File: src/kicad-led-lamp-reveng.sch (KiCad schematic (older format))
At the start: 18 parts, among them J1 AC2, J2 AC1, J3 L+, J4 L-, SW1 SW_Push_SPDT

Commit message: Finished pcb layout
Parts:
- C1: footprint (none) -> igorkelvin:C_Polyester_11.20mm_4.9mm
- C2: footprint (none) -> igorkelvin:C_Polyester_21.80mm_7.10mm
- D1, D3, D4, D5, D6: footprint Resistor_THT:R_Axial_DIN0207_L6.3mm_D2.5mm_P7.62mm_Horizontal -> igorkelvin:DIODE_Axial_DIN0207_L6.3mm_D2.5mm_P7.62mm_Horizontal
- J1, J2, J3, J4: footprint (none) -> Connector_PinHeader_2.54mm:PinHeader_1x01_P2.54mm_Vertical
- SW1: footprint (none) -> igorkelvin:Switch_4-Way
- renumbered R3 to R1, R1 to R3
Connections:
- net at C1.2, C2.2, D1.1 (K)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: no longer D5.2 (A), R4.2
- new net: D5.2 (A), R4.2
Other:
- moved on the sheet: C1, C2, C3, D1, D2, D3, D4, D5, D6, J1, J2, J3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

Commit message: Schematics rearrangement, changed C3 polarity and Rev1 for pcb & sch
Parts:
- C1: value 220nF_400V_Polyester -> 220nF
- C2: value 1uF_400V_Polyester -> 1uF
- C3: value 6.8uF_400V_Electrolytic -> 6.8uF
- D2: value LED_ALT -> LED
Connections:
- net at D1.2 (A), D2.1 (K), J4.1 (Pin_1)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: now also C3.2, D3.1 (K); no longer C3.1, D3.2 (A)
- net at D4.1 (K), D6.1 (K), J3.1 (Pin_1)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: now also C3.1; no longer C3.2
- net at D4.2 (A), J2.1 (Pin_1): now also D3.2 (A); no longer D3.1 (K)
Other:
- moved on the sheet: C1, C2, C3, D1, D2, D3, D4, D5, D6, J1, J2, J3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

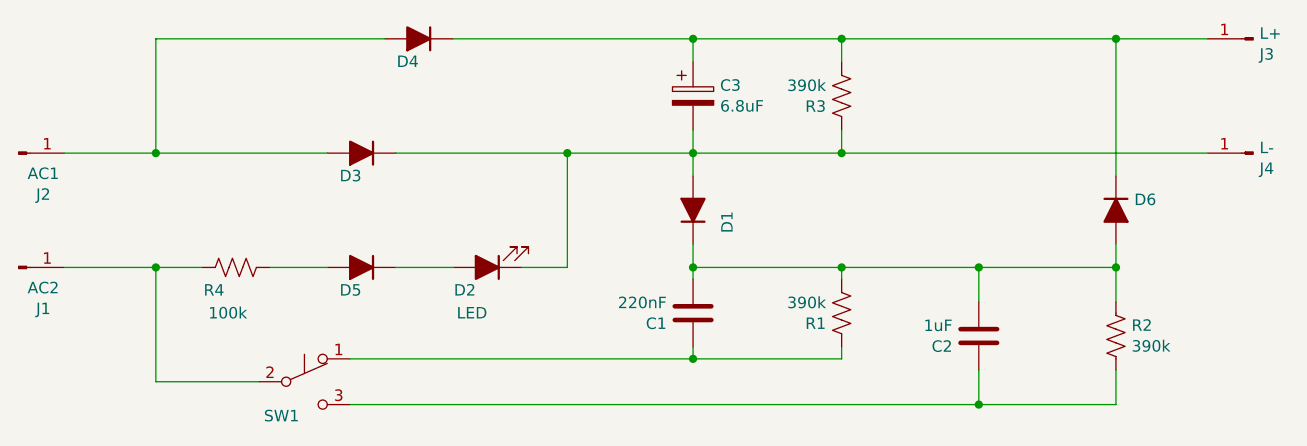
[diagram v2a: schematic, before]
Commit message: Corrected D3 and PCB filled zones
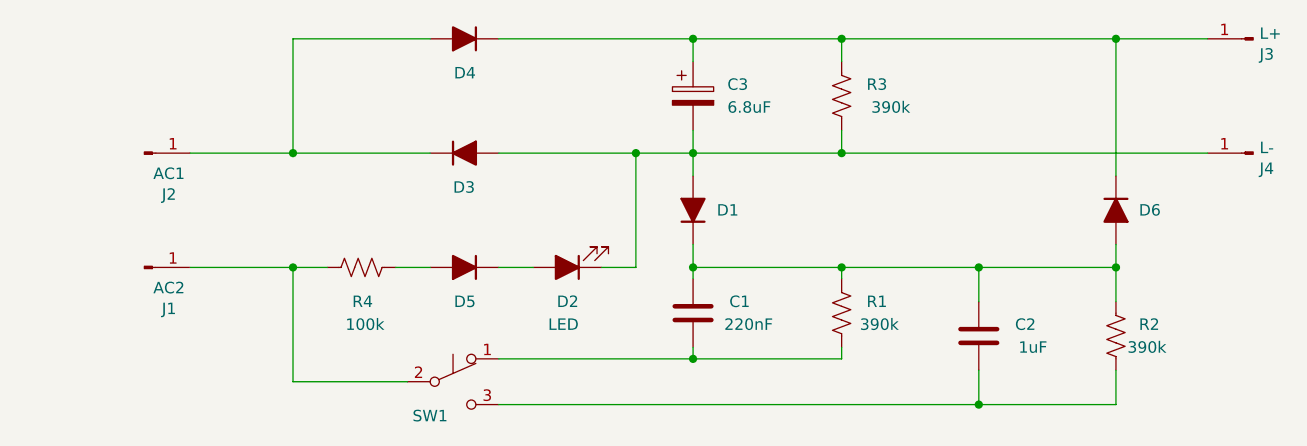
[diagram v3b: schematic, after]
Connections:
- net at C3.2, D1.2 (A), D2.1 (K)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: now also D3.2 (A); no longer D3.1 (K)
- net at D4.2 (A), J2.1 (Pin_1): now also D3.1 (K); no longer D3.2 (A)
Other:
- moved on the sheet: D2, D3, D4, D5, J1, J2, R4, SW1
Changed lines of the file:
@@
 Title "LED Lamp Rev. Engineering"
 Date "2020-08-04"
-Rev "0"
+Rev "1"
 Comp "CEFET/RJ"
 Comment1 "Igor Kelvin <igorkelvin@gmail.com>"
@@
 L Device:D_ALT D3
 U 1 1 5F298B6A
-P 3350 2450
-F 0 "D3" H 3350 2550 50  0000 L CNN
-F 1 "1N4007" V 3395 2530 50  0001 L CNN
-F 2 "igorkelvin:DIODE_Axial_DIN0207_L6.3mm_D2.5mm_P7.62mm_Horizontal" H 3350 2450 50  0001 C CNN
-F 3 "~" H 3350 2450 50  0001 C CNN
-	1    3350 2450
-	-1   0    0    1
+P 3800 2450
+F 0 "D3" H 3750 2300 50  0000 L CNN
+F 1 "1N4007" V 3845 2530 50  0001 L CNN
+F 2 "igorkelvin:DIODE_Axial_DIN0207_L6.3mm_D2.5mm_P7.62mm_Horizontal" H 3800 2450 50  0001 C CNN
+F 3 "~" H 3800 2450 50  0001 C CNN
+	1    3800 2450
+	1    0    0    -1
 $EndComp
 $Comp
@@
 U 1 1 5F29AE02
 P 5450 3150
-F 0 "R1" H 5518 3196 50  0000 L CNN
-F 1 "390k" H 5518 3105 50  0000 L CNN
+F 0 "R1" H 5250 3100 50  0000 L CNN
+F 1 "390k" H 5200 3200 50  0000 L CNN
 F 2 "Resistor_THT:R_Axial_DIN0207_L6.3mm_D2.5mm_P7.62mm_Horizontal" V 5490 3140 50  0001 C CNN
 F 3 "~" H 5450 3150 50  0001 C CNN
@@
 $EndComp
 $Comp
-L Connector:Conn_01x01_Male J2
-U 1 1 5F2EAC7D
-P 1850 2450
-F 0 "J2" H 1958 2631 50  0000 C CNN
-F 1 "AC1" H 1958 2540 50  0000 C CNN
-F 2 "Connector_PinHeader_2.54mm:PinHeader_1x01_P2.54mm_Vertical" H 1850 2450 50  0001 C CNN
-F 3 "~" H 1850 2450 50  0001 C CNN
-	1    1850 2450
-	1    0    0    1
-$EndComp
-$Comp
-L Connector:Conn_01x01_Male J1
-U 1 1 5F2EB389
-P 1850 2950
-F 0 "J1" H 1958 3131 50  0000 C CNN
-F 1 "AC2" H 1958 3040 50  0000 C CNN
-F 2 "Connector_PinHeader_2.54mm:PinHeader_1x01_P2.54mm_Vertical" H 1850 2950 50  0001 C CNN
-F 3 "~" H 1850 2950 50  0001 C CNN
-	1    1850 2950
-	1    0    0    1
-$EndComp
-$Comp
-L Device:LED_ALT D2
-U 1 1 5F29941E
-P 3900 2950
-F 0 "D2" H 3950 3050 50  0000 L CNN
-F 1 "LED" H 3900 3150 50  0000 L CNN
-F 2 "LED_THT:LED_D3.0mm" H 3900 2950 50  0001 C CNN
-F 3 "~" H 3900 2950 50  0001 C CNN
-	1    3900 2950
-	-1   0    0    1
-$EndComp
-$Comp
 L Connector:Conn_01x01_Male J4
 U 1 1 5F2ED558
@@
 U 1 1 5F2984DE
 P 4800 2700
-F 0 "D1" H 4700 2550 50  0000 L CNN
+F 0 "D1" V 4800 2500 50  0000 L CNN
 F 1 "1N4007" H 4700 2450 50  0001 L CNN
 F 2 "igorkelvin:DIODE_Axial_DIN0207_L6.3mm_D2.5mm_P7.62mm_Horizontal" H 4800 2700 50  0001 C CNN
@@
 L Device:R_US R4
 U 1 1 5F29B09B
-P 2800 2950
-F 0 "R4" V 2700 3000 50  0000 L CNN
-F 1 "100k" V 2600 2900 50  0000 L CNN
-F 2 "Resistor_THT:R_Axial_DIN0207_L6.3mm_D2.5mm_P7.62mm_Horizontal" V 2840 2940 50  0001 C CNN
-F 3 "~" H 2800 2950 50  0001 C CNN
-	1    2800 2950
+P 3350 2950
+F 0 "R4" V 3200 2900 50  0000 L CNN
+F 1 "100k" V 3100 2850 50  0000 L CNN
+F 2 "Resistor_THT:R_Axial_DIN0207_L6.3mm_D2.5mm_P7.62mm_Horizontal" V 3390 2940 50  0001 C CNN
+F 3 "~" H 3350 2950 50  0001 C CNN
+	1    3350 2950
 	0    -1   -1   0
 $EndComp
 Wire Wire Line
-	2450 2950 2450 3450
-Wire Wire Line
-	2450 3450 2900 3450
+	3050 2950 3050 3450
+Wire Wire Line
+	3050 3450 3550 3450
 $Comp
 L Device:C C1
 U 1 1 5F297900
 P 4800 3150
-F 0 "C1" H 4915 3196 50  0000 L CNN
-F 1 "220nF" H 4915 3105 50  0000 L CNN
+F 0 "C1" H 4550 3100 50  0000 L CNN
+F 1 "220nF" H 4450 3200 50  0000 L CNN
 F 2 "igorkelvin:C_Polyester_11.20mm_4.9mm" H 4838 3000 50  0001 C CNN
 F 3 "~" H 4800 3150 50  0001 C CNN
@@
 U 1 1 5F298A12
 P 6650 2700
-F 0 "D6" V 6604 2780 50  0000 L CNN
+F 0 "D6" V 6650 2800 50  0000 L CNN
 F 1 "1N4007" V 6695 2780 50  0001 L CNN
 F 2 "igorkelvin:DIODE_Axial_DIN0207_L6.3mm_D2.5mm_P7.62mm_Horizontal" H 6650 2700 50  0001 C CNN
@@
 $EndComp
 $Comp
-L Device:D_ALT D4
-U 1 1 5F2986FE
-P 3600 1950
-F 0 "D4" H 3600 2050 50  0000 L CNN
-F 1 "1N4007" V 3645 2030 50  0001 L CNN
-F 2 "igorkelvin:DIODE_Axial_DIN0207_L6.3mm_D2.5mm_P7.62mm_Horizontal" H 3600 1950 50  0001 C CNN
-F 3 "~" H 3600 1950 50  0001 C CNN
-	1    3600 1950
-	-1   0    0    1
-$EndComp
-Wire Wire Line
-	4250 2450 4800 2450
-Wire Wire Line
-	2450 1950 3450 1950
-$Comp
 L Device:CP C3
 U 1 1 5F296AB3
 P 4800 2200
-F 0 "C3" H 4918 2246 50  0000 L CNN
-F 1 "6.8uF" H 4918 2155 50  0000 L CNN
+F 0 "C3" H 4950 2250 50  0000 L CNN
+F 1 "6.8uF" H 4950 2150 50  0000 L CNN
 F 2 "Capacitor_THT:CP_Radial_D8.0mm_P5.00mm" H 4838 2050 50  0001 C CNN
 F 3 "~" H 4800 2200 50  0001 C CNN
@@
 U 1 1 5F299F5C
 P 5450 2200
-F 0 "R3" H 5518 2246 50  0000 L CNN
-F 1 "390k" H 5518 2155 50  0000 L CNN
+F 0 "R3" H 5250 2150 50  0000 L CNN
+F 1 "390k" H 5150 2250 50  0000 L CNN
 F 2 "Resistor_THT:R_Axial_DIN0207_L6.3mm_D2.5mm_P7.62mm_Horizontal" V 5490 2190 50  0001 C CNN
 F 3 "~" H 5450 2200 50  0001 C CNN
@@
 L Switch:SW_Push_SPDT SW1
 U 1 1 5F29E74E
-P 3100 3450
-F 0 "SW1" H 3000 3300 50  0000 C CNN
-F 1 "SW_Push_SPDT" H 3100 3644 50  0001 C CNN
-F 2 "igorkelvin:Switch_4-Way" H 3100 3450 50  0001 C CNN
-F 3 "~" H 3100 3450 50  0001 C CNN
-	1    3100 3450
+P 3750 3450
+F 0 "SW1" H 3650 3300 50  0000 C CNN
+F 1 "SW_Push_SPDT" H 3750 3644 50  0001 C CNN
+F 2 "igorkelvin:Switch_4-Way" H 3750 3450 50  0001 C CNN
+F 3 "~" H 3750 3450 50  0001 C CNN
+	1    3750 3450
 	1    0    0    -1
 $EndComp
@@
 	4800 3350 5450 3350
 Wire Wire Line
-	3500 2450 4250 2450
-Wire Wire Line
-	2450 2450 3200 2450
-Connection ~ 2450 2450
-Wire Wire Line
-	2450 2450 2450 1950
-Wire Wire Line
-	2450 2950 2650 2950
-Wire Wire Line
-	4050 2950 4250 2950
-Wire Wire Line
-	4250 2950 4250 2450
-Connection ~ 4250 2450
-Connection ~ 2450 2950
+	3050 2450 3650 2450
+Connection ~ 3050 2450
+Wire Wire Line
+	3050 2450 3050 1950
+Wire Wire Line
+	3050 2950 3200 2950
+Connection ~ 3050 2950
 Wire Wire Line
 	6650 2950 6650 2850
@@
 	4800 2450 5450 2450
 Wire Wire Line
-	3750 1950 4800 1950
-Wire Wire Line
 	4800 2050 4800 1950
 Connection ~ 4800 1950
@@
 Wire Wire Line
 	4800 1950 5450 1950
-Wire Wire Line
-	3200 2950 2950 2950
-Wire Wire Line
-	3500 2950 3750 2950
-$Comp
-L Device:D_ALT D5
-U 1 1 5F2A91F2
-P 3350 2950
-F 0 "D5" H 3350 3050 50  0000 L CNN
-F 1 "1N4007" H 3250 3050 50  0001 L CNN
-F 2 "igorkelvin:DIODE_Axial_DIN0207_L6.3mm_D2.5mm_P7.62mm_Horizontal" H 3350 2950 50  0001 C CNN
-F 3 "~" H 3350 2950 50  0001 C CNN
-	1    3350 2950
-	-1   0    0    1
-$EndComp
 Wire Wire Line
 	4800 2950 5450 2950
@@
 U 1 1 5F29AC14
 P 6650 3250
-F 0 "R2" H 6718 3296 50  0000 L CNN
-F 1 "390k" H 6718 3205 50  0000 L CNN
+F 0 "R2" H 6750 3300 50  0000 L CNN
+F 1 "390k" H 6700 3200 50  0000 L CNN
 F 2 "Resistor_THT:R_Axial_DIN0207_L6.3mm_D2.5mm_P7.62mm_Horizontal" V 6690 3240 50  0001 C CNN
 F 3 "~" H 6650 3250 50  0001 C CNN
@@
 	5450 2950 5450 3000
 Wire Wire Line
-	3300 3350 4800 3350
+	3950 3350 4800 3350
 Connection ~ 4800 3350
 Wire Wire Line
-	3300 3550 6050 3550
+	3950 3550 6050 3550
 Wire Wire Line
 	6650 3400 6650 3550
@@
 U 1 1 5F296DBF
 P 6050 3250
-F 0 "C2" H 6165 3296 50  0000 L CNN
-F 1 "1uF" H 6165 3205 50  0000 L CNN
+F 0 "C2" H 5800 3200 50  0000 L CNN
+F 1 "1uF" H 5750 3300 50  0000 L CNN
 F 2 "igorkelvin:C_Polyester_21.80mm_7.10mm" H 6088 3100 50  0001 C CNN
 F 3 "~" H 6050 3250 50  0001 C CNN
@@
 $EndComp
 Wire Wire Line
-	2050 2950 2450 2950
-Wire Wire Line
-	2050 2450 2450 2450
+	2600 2450 3050 2450
+$Comp
+L Connector:Conn_01x01_Male J2
+U 1 1 5F2EAC7D
+P 2400 2450
+F 0 "J2" H 2508 2631 50  0000 C CNN
+F 1 "AC1" H 2508 2540 50  0000 C CNN
+F 2 "Connector_PinHeader_2.54mm:PinHeader_1x01_P2.54mm_Vertical" H 2400 2450 50  0001 C CNN
+F 3 "~" H 2400 2450 50  0001 C CNN
+	1    2400 2450
+	1    0    0    1
+$EndComp
+Wire Wire Line
+	2600 2950 3050 2950
+$Comp
+L Connector:Conn_01x01_Male J1
+U 1 1 5F2EB389
+P 2400 2950
+F 0 "J1" H 2508 3131 50  0000 C CNN
+F 1 "AC2" H 2508 3040 50  0000 C CNN
+F 2 "Connector_PinHeader_2.54mm:PinHeader_1x01_P2.54mm_Vertical" H 2400 2950 50  0001 C CNN
+F 3 "~" H 2400 2950 50  0001 C CNN
+	1    2400 2950
+	1    0    0    1
+$EndComp
+Wire Wire Line
+	3050 1950 3650 1950
+Wire Wire Line
+	3950 1950 4800 1950
+$Comp
+L Device:D_ALT D4
+U 1 1 5F2986FE
+P 3800 1950
+F 0 "D4" H 3750 2100 50  0000 L CNN
+F 1 "1N4007" V 3845 2030 50  0001 L CNN
+F 2 "igorkelvin:DIODE_Axial_DIN0207_L6.3mm_D2.5mm_P7.62mm_Horizontal" H 3800 1950 50  0001 C CNN
+F 3 "~" H 3800 1950 50  0001 C CNN
+	1    3800 1950
+	-1   0    0    1
+$EndComp
+Wire Wire Line
+	3650 2950 3500 2950
+$Comp
+L Device:D_ALT D5
+U 1 1 5F2A91F2
+P 3800 2950
+F 0 "D5" H 3750 3100 50  0000 L CNN
+F 1 "1N4007" H 3700 3050 50  0001 L CNN
+F 2 "igorkelvin:DIODE_Axial_DIN0207_L6.3mm_D2.5mm_P7.62mm_Horizontal" H 3800 2950 50  0001 C CNN
+F 3 "~" H 3800 2950 50  0001 C CNN
+	1    3800 2950
+	-1   0    0    1
+$EndComp
+Wire Wire Line
+	3950 2950 4100 2950
+$Comp
+L Device:LED_ALT D2
+U 1 1 5F29941E
+P 4250 2950
+F 0 "D2" H 4200 3100 50  0000 L CNN
+F 1 "LED" H 4200 3200 50  0000 L CNN
+F 2 "LED_THT:LED_D3.0mm" H 4250 2950 50  0001 C CNN
+F 3 "~" H 4250 2950 50  0001 C CNN
+	1    4250 2950
+	-1   0    0    1
+$EndComp
+Wire Wire Line
+	3950 2450 4550 2450
+Wire Wire Line
+	4550 2450 4800 2450
+Connection ~ 4550 2450
+Wire Wire Line
+	4400 2950 4550 2950
+Wire Wire Line
+	4550 2950 4550 2450
 $EndSCHEMATC
